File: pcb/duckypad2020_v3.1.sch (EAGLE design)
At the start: 108 parts, among them IC1 STM32F072C8T6, IC2 REG1117, IC3 74AHCT1G08DBV, SW1 324_SW324_SWITCH_FOOT_HOLE, SW10 KAILH_SWITCH_SOCKET_KAILH_SWI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, SW11 KAILH_SWITCH_SOCKET_KAILH_SWI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, SW12 KAILH_SWITCH_SOCKET_KAILH_SWI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, SW13 KAILH_SWITCH_SOCKET_KAILH_SWI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, SW14 KAILH_SWITCH_SOCKET_KAILH_SWI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, SW15 KAILH_SWITCH_SOCKET_KAILH_SWI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

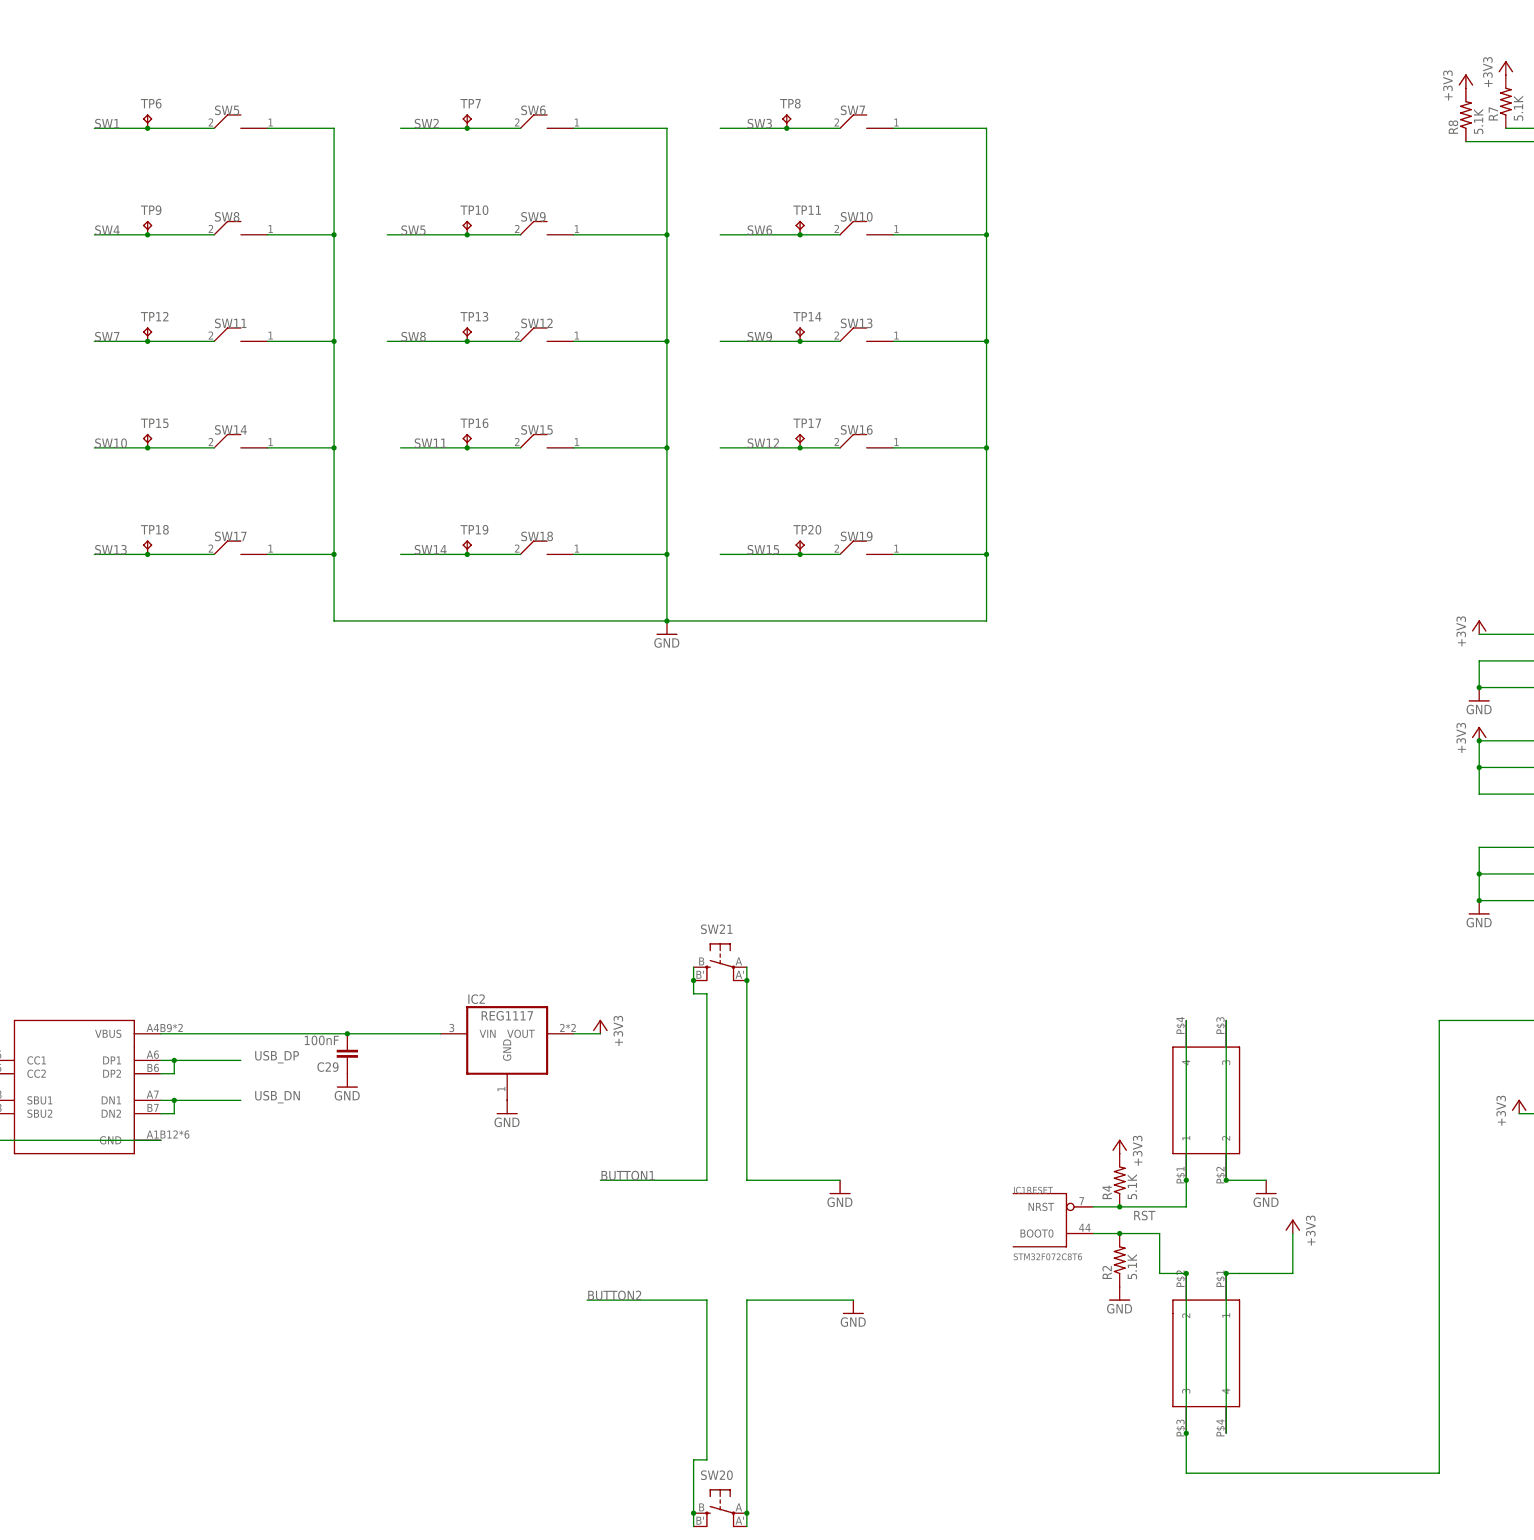
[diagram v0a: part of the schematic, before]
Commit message: finished hw socket vias, spare header on BOOT0
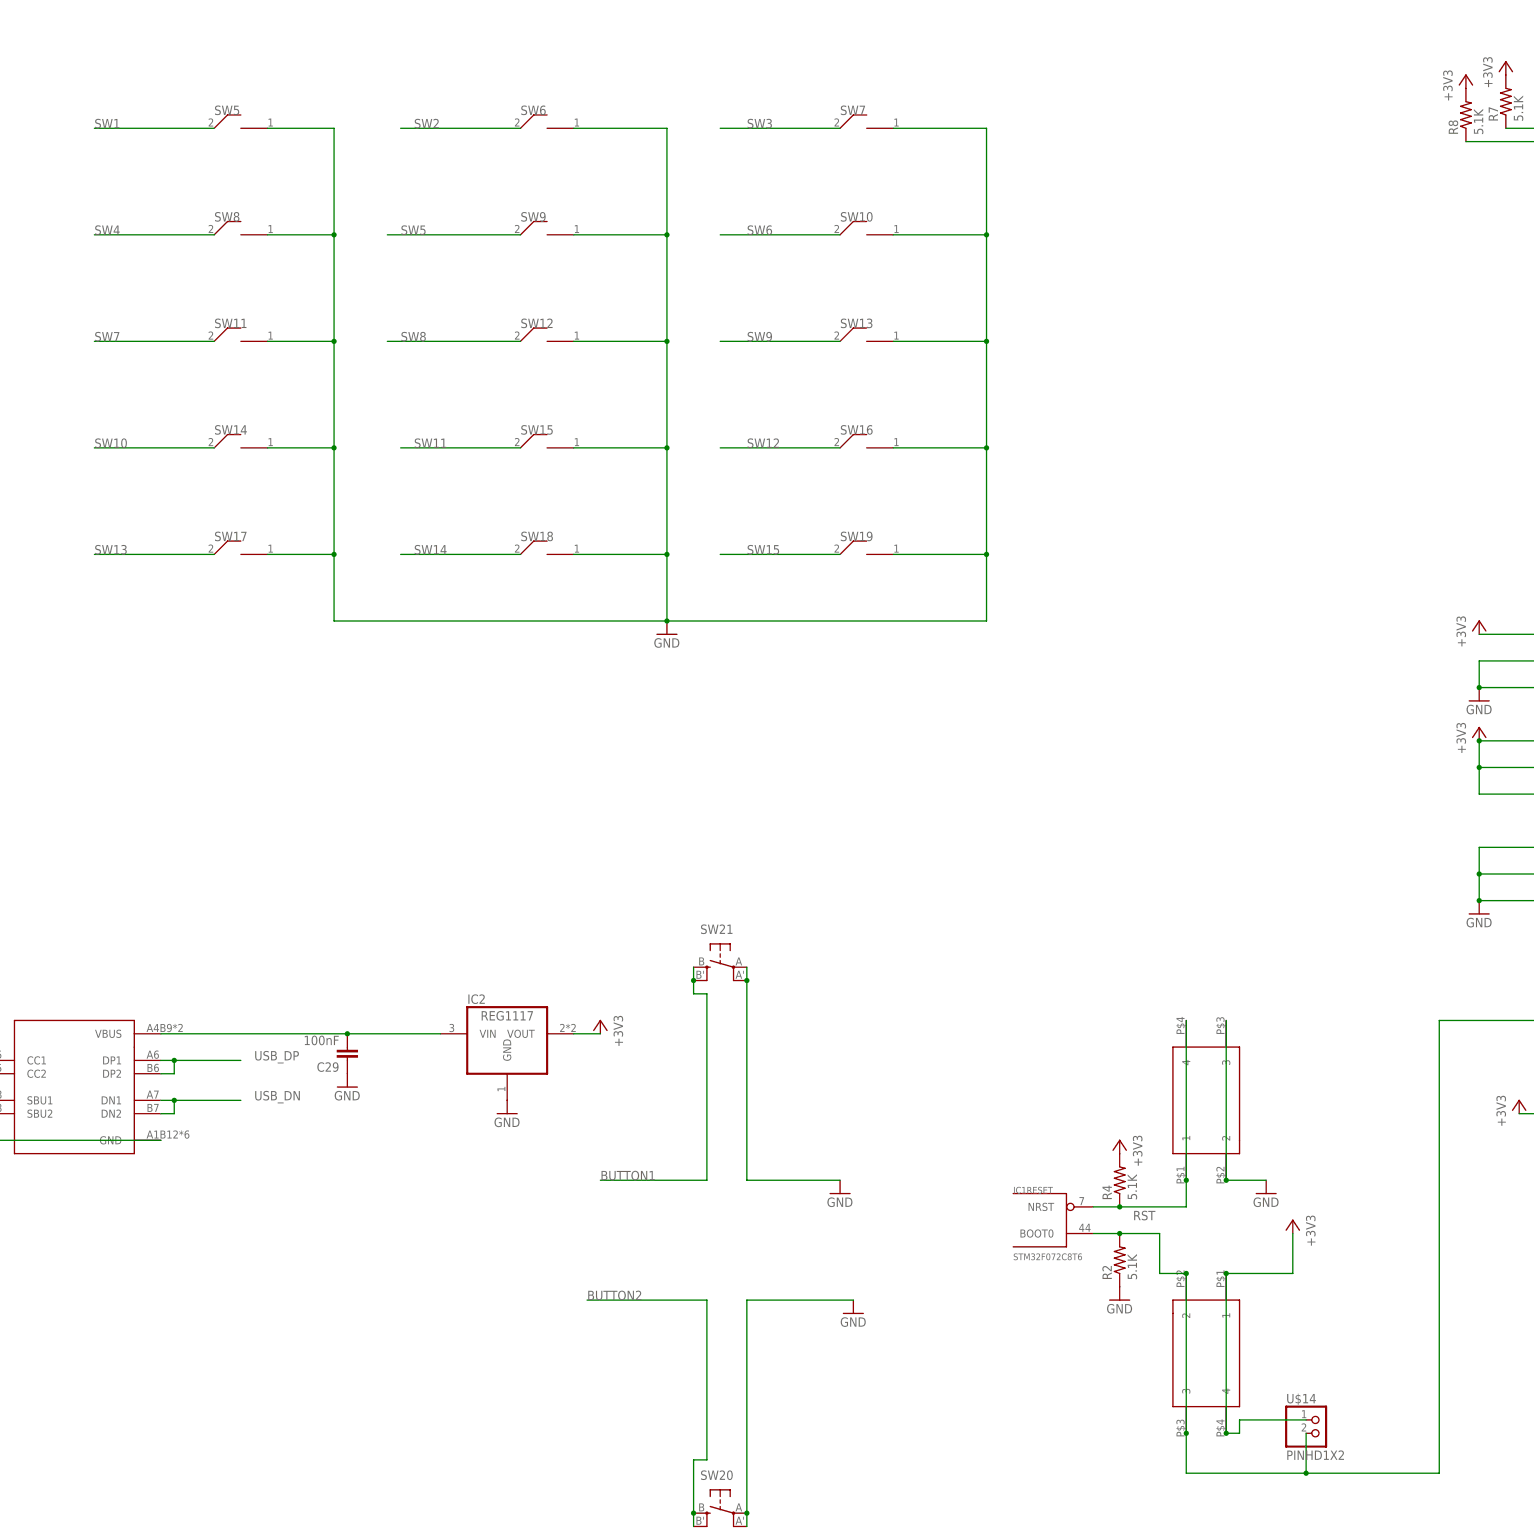
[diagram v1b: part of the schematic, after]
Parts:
- removed TP10, TP11, TP12, TP13, TP14, TP15, TP16, TP17, TP18, TP19, TP20, TP6, TP7, TP8, TP9: TPTP15R, testpad:TPTP15R
- added U$14: PINHD1X2, adafruit_changed:PINHD1X2
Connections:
- net +3V3: now also U$14.1
- net BUTTON_DEBUG: now also U$14.2
- net SW1: no longer TP6.TP
- net SW10: no longer TP15.TP
- net SW11: no longer TP16.TP
- net SW12: no longer TP17.TP
- net SW13: no longer TP18.TP
- net SW14: no longer TP19.TP
- net SW15: no longer TP20.TP
- net SW2: no longer TP7.TP
- net SW3: no longer TP8.TP
- net SW4: no longer TP9.TP
- net SW5: no longer TP10.TP
- net SW6: no longer TP11.TP
- net SW7: no longer TP12.TP
- net SW8: no longer TP13.TP
- net SW9: no longer TP14.TP
